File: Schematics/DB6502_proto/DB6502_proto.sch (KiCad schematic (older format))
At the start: 22 parts, among them SW1 Reset, U1 DS1813, U10 28C256, U11 22V10C, U2 74AC32, U3 65C02S, U4 74AC04, U5 62256, U6 74HC74, U7 74AC08, U8 62256, U9 74AC138, X1 14MHz

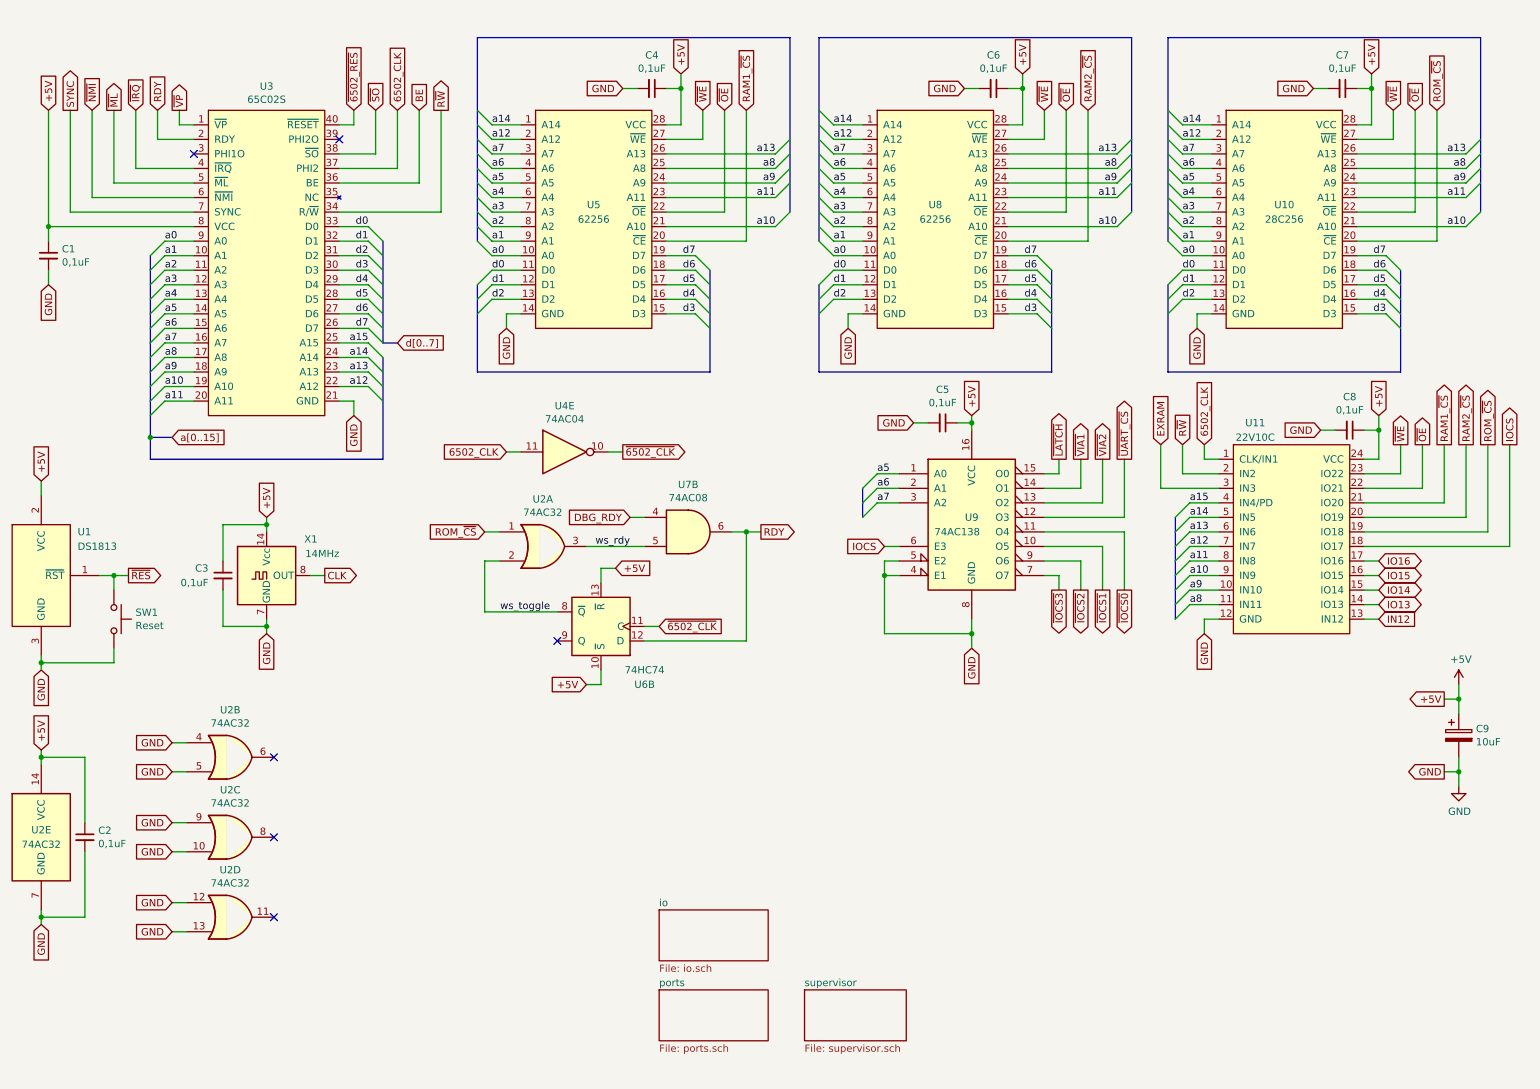
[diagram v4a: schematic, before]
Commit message: Fixed issue with UART CEN during low clock, added IRQ gate
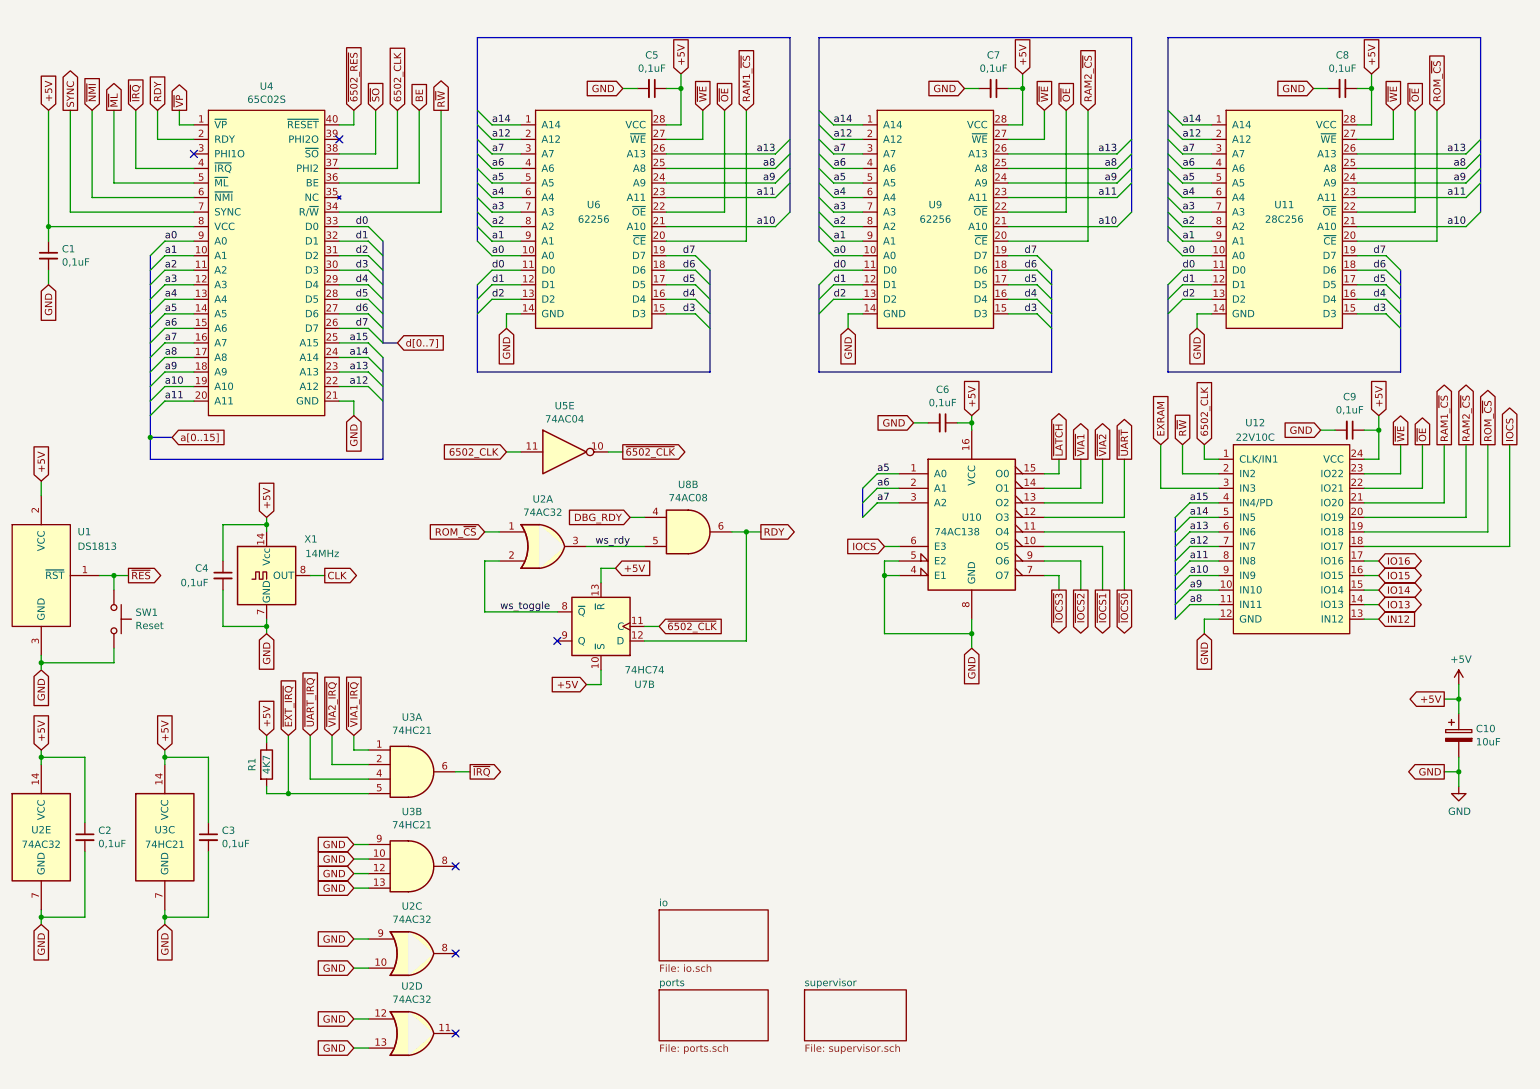
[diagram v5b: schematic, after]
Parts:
- removed unit 2 of U2
- added C3: 0,1uF, symbol Device:C_Small
- added R1: 4K7, symbol Device:R
- added U3: 74HC21, symbol 74xx:74LS21
- renumbered C9 to C10, C3 to C4, C4 to C5, C5 to C6, C6 to C7, C7 to C8, C8 to C9, U9 to U10, U10 to U11, U11 to U12, U3 to U4, U4 to U5, U5 to U6, U6 to U7, U7 to U8, U8 to U9
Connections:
- net +5V: now also C3.1, R1.1, U3.14 (VCC)
- net GND: now also C3.2, U3.10, U3.12, U3.13, U3.7 (GND), U3.9
- net ~IRQ: now also U3.6
- net ~UART_CS renamed ~UART
- new net ~EXT_IRQ: R1.2, U3.5
- new net ~UART_IRQ: U3.4
- new net ~VIA1_IRQ: U3.1
- new net ~VIA2_IRQ: U3.2
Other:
- moved on the sheet: U2C, U2D
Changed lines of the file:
@@
 	10600 5200 10600 5300
 $Comp
-L 6502:22V10C U11
+L 6502:22V10C U12
 U 1 1 5F680A6E
 P 9450 4100
-F 0 "U11" H 9200 4900 50  0000 C CNN
+F 0 "U12" H 9200 4900 50  0000 C CNN
 F 1 "22V10C" H 9200 4800 50  0000 C CNN
 F 2 "Package_DIP:DIP-24_W7.62mm_Socket" H 9450 3400 50  0001 C CNN
@@
 	8150 3850 7750 3850
 Text GLabel 8300 3550 1    50   Output ~ 0
-~UART_CS
+~UART
 Wire Wire Line
 	8300 3550 8300 3950
@@
 Connection ~ 1350 4350
 $Comp
-L 74xx:74LS138 U9
+L 74xx:74LS138 U10
 U 1 1 5F9A1F2C
 P 7250 3950
-F 0 "U9" H 7250 3950 50  0000 C CNN
+F 0 "U10" H 7250 3950 50  0000 C CNN
 F 1 "74AC138" H 7150 3850 50  0000 C CNN
 F 2 "Package_DIP:DIP-16_W7.62mm_Socket" H 7250 3950 50  0001 C CNN
@@
 $EndComp
 $Comp
-L 6502:65C02S U3
+L 6502:65C02S U4
 U 1 1 5F5A65C1
 P 2400 2150
-F 0 "U3" H 2400 3315 50  0000 C CNN
+F 0 "U4" H 2400 3315 50  0000 C CNN
 F 1 "65C02S" H 2400 3224 50  0000 C CNN
 F 2 "Package_DIP:DIP-40_W15.24mm_Socket" H 2400 3200 50  0001 C CNN
@@
 $EndComp
 $Comp
-L 6502:62256 U8
+L 6502:62256 U9
 U 1 1 5F5FD943
 P 7000 1900
-F 0 "U8" H 7000 2000 50  0000 C CNN
+F 0 "U9" H 7000 2000 50  0000 C CNN
 F 1 "62256" H 7000 1900 50  0000 C CNN
 F 2 "Package_DIP:DIP-28_W15.24mm_Socket" H 6950 2700 50  0001 C CNN
@@
 $EndComp
 $Comp
-L 6502:62256 U5
+L 6502:62256 U6
 U 1 1 5F5BE432
 P 4650 1900
-F 0 "U5" H 4650 2000 50  0000 C CNN
+F 0 "U6" H 4650 2000 50  0000 C CNN
 F 1 "62256" H 4650 1900 50  0000 C CNN
 F 2 "Package_DIP:DIP-28_W15.24mm_Socket" H 4600 2700 50  0001 C CNN
@@
 $EndComp
 $Comp
-L 6502:28C256 U10
+L 6502:28C256 U11
 U 1 1 5F605CEF
 P 9400 1900
-F 0 "U10" H 9400 2000 50  0000 C CNN
+F 0 "U11" H 9400 2000 50  0000 C CNN
 F 1 "28C256" H 9400 1900 50  0000 C CNN
 F 2 "Package_DIP:DIP-28_W15.24mm_Socket" H 9350 2700 50  0001 C CNN
@@
 P 4450 3500
 AR Path="/5F8F4E1E/5FD6D1DD" Ref="U?"  Part="5"
-AR Path="/5FD6D1DD" Ref="U4"  Part="5"
-F 0 "U4" H 4450 3817 50  0000 C CNN
+AR Path="/5FD6D1DD" Ref="U5"  Part="5"
+F 0 "U5" H 4450 3817 50  0000 C CNN
 F 1 "74AC04" H 4450 3726 50  0000 C CNN
 F 2 "" H 4450 3500 50  0001 C CNN
@@
 P 5300 4050
 AR Path="/5F8F4E1E/5FDA6F78" Ref="U?"  Part="2"
-AR Path="/5FDA6F78" Ref="U7"  Part="2"
-F 0 "U7" H 5300 4375 50  0000 C CNN
+AR Path="/5FDA6F78" Ref="U8"  Part="2"
+F 0 "U8" H 5300 4375 50  0000 C CNN
 F 1 "74AC08" H 5300 4284 50  0000 C CNN
 F 2 "" H 5300 4050 50  0001 C CNN
@@
 P 4700 4700
 AR Path="/5F8F4E1E/5FE3D22B" Ref="U?"  Part="2"
-AR Path="/5FE3D22B" Ref="U6"  Part="2"
-F 0 "U6" H 4400 5100 50  0000 C CNN
+AR Path="/5FE3D22B" Ref="U7"  Part="2"
+F 0 "U7" H 4400 5100 50  0000 C CNN
 F 1 "74HC74" H 4400 5000 50  0000 C CNN
 F 2 "" H 4700 4700 50  0001 C CNN
@@
 	900  2350 900  2250
 $Comp
-L Device:C_Small C4
+L Device:C_Small C5
 U 1 1 6006C4BF
 P 5050 1000
-F 0 "C4" V 4821 1000 50  0000 C CNN
+F 0 "C5" V 4821 1000 50  0000 C CNN
 F 1 "0,1uF" V 4912 1000 50  0000 C CNN
 F 2 "" H 5050 1000 50  0001 C CNN
@@
 	4850 1000 4950 1000
 $Comp
-L Device:C_Small C6
+L Device:C_Small C7
 U 1 1 600A0144
 P 7400 1000
-F 0 "C6" V 7171 1000 50  0000 C CNN
+F 0 "C7" V 7171 1000 50  0000 C CNN
 F 1 "0,1uF" V 7262 1000 50  0000 C CNN
 F 2 "" H 7400 1000 50  0001 C CNN
@@
 	7200 1000 7300 1000
 $Comp
-L Device:C_Small C7
+L Device:C_Small C8
 U 1 1 600B9F0E
 P 9800 1000
-F 0 "C7" V 9571 1000 50  0000 C CNN
+F 0 "C8" V 9571 1000 50  0000 C CNN
 F 1 "0,1uF" V 9662 1000 50  0000 C CNN
 F 2 "" H 9800 1000 50  0001 C CNN
@@
 +5V
 $Comp
-L Device:C_Small C8
+L Device:C_Small C9
 U 1 1 600EDE42
 P 9850 3350
-F 0 "C8" V 9621 3350 50  0000 C CNN
+F 0 "C9" V 9621 3350 50  0000 C CNN
 F 1 "0,1uF" V 9712 3350 50  0000 C CNN
 F 2 "" H 9850 3350 50  0001 C CNN
@@
 	10050 3350 10050 3250
 $Comp
-L Device:C_Small C5
+L Device:C_Small C6
 U 1 1 60156577
 P 7050 3300
-F 0 "C5" V 6821 3300 50  0000 C CNN
+F 0 "C6" V 6821 3300 50  0000 C CNN
 F 1 "0,1uF" V 6912 3300 50  0000 C CNN
 F 2 "" H 7050 3300 50  0001 C CNN
@@
 	7250 3300 7250 3350
 $Comp
-L Device:C_Small C3
+L Device:C_Small C4
 U 1 1 601720DC
 P 2100 4350
-F 0 "C3" H 2000 4400 50  0000 R CNN
+F 0 "C4" H 2000 4400 50  0000 R CNN
 F 1 "0,1uF" H 2000 4300 50  0000 R CNN
 F 2 "" H 2100 4350 50  0001 C CNN
@@
 $Comp
 L 74xx:74LS32 U2
-U 2 1 60312905
-P 2150 5600
-F 0 "U2" H 2150 5925 50  0000 C CNN
-F 1 "74AC32" H 2150 5834 50  0000 C CNN
-F 2 "" H 2150 5600 50  0001 C CNN
-F 3 "http://www.ti.com/lit/gpn/sn74LS32" H 2150 5600 50  0001 C CNN
-	2    2150 5600
-	1    0    0    -1
-$EndComp
-Text GLabel 1750 5500 0    50   Input ~ 0
-GND
-Text GLabel 1750 5700 0    50   Input ~ 0
-GND
-Wire Wire Line
-	1750 5700 1850 5700
-Wire Wire Line
-	1750 5500 1850 5500
-NoConn ~ 2450 5600
-$Comp
-L 74xx:74LS32 U2
 U 3 1 603ACD27
-P 2150 6150
-F 0 "U2" H 2150 6475 50  0000 C CNN
-F 1 "74AC32" H 2150 6384 50  0000 C CNN
-F 2 "" H 2150 6150 50  0001 C CNN
-F 3 "http://www.ti.com/lit/gpn/sn74LS32" H 2150 6150 50  0001 C CNN
-	3    2150 6150
-	1    0    0    -1
-$EndComp
-Text GLabel 1750 6050 0    50   Input ~ 0
-GND
-Text GLabel 1750 6250 0    50   Input ~ 0
-GND
-Wire Wire Line
-	1750 6250 1850 6250
-Wire Wire Line
-	1750 6050 1850 6050
-NoConn ~ 2450 6150
+P 3400 6950
+F 0 "U2" H 3400 7275 50  0000 C CNN
+F 1 "74AC32" H 3400 7184 50  0000 C CNN
+F 2 "" H 3400 6950 50  0001 C CNN
+F 3 "http://www.ti.com/lit/gpn/sn74LS32" H 3400 6950 50  0001 C CNN
+	3    3400 6950
+	1    0    0    -1
+$EndComp
+Text GLabel 3000 6850 0    50   Input ~ 0
+GND
+Text GLabel 3000 7050 0    50   Input ~ 0
+GND
+Wire Wire Line
+	3000 7050 3100 7050
+Wire Wire Line
+	3000 6850 3100 6850
+NoConn ~ 3700 6950
 $Comp
 L 74xx:74LS32 U2
 U 4 1 603CCE1F
-P 2150 6700
-F 0 "U2" H 2150 7025 50  0000 C CNN
-F 1 "74AC32" H 2150 6934 50  0000 C CNN
-F 2 "" H 2150 6700 50  0001 C CNN
-F 3 "http://www.ti.com/lit/gpn/sn74LS32" H 2150 6700 50  0001 C CNN
-	4    2150 6700
-	1    0    0    -1
-$EndComp
-Text GLabel 1750 6600 0    50   Input ~ 0
-GND
-Text GLabel 1750 6800 0    50   Input ~ 0
-GND
-Wire Wire Line
-	1750 6800 1850 6800
-Wire Wire Line
-	1750 6600 1850 6600
-NoConn ~ 2450 6700
-$Comp
-L Device:CP C9
+P 3400 7500
+F 0 "U2" H 3400 7825 50  0000 C CNN
+F 1 "74AC32" H 3400 7734 50  0000 C CNN
+F 2 "" H 3400 7500 50  0001 C CNN
+F 3 "http://www.ti.com/lit/gpn/sn74LS32" H 3400 7500 50  0001 C CNN
+	4    3400 7500
+	1    0    0    -1
+$EndComp
+Text GLabel 3000 7400 0    50   Input ~ 0
+GND
+Text GLabel 3000 7600 0    50   Input ~ 0
+GND
+Wire Wire Line
+	3000 7600 3100 7600
+Wire Wire Line
+	3000 7400 3100 7400
+NoConn ~ 3700 7500
+$Comp
+L Device:CP C10
 U 1 1 5F613640
 P 10600 5450
-F 0 "C9" H 10718 5496 50  0000 L CNN
+F 0 "C10" H 10718 5496 50  0000 L CNN
 F 1 "10uF" H 10718 5405 50  0000 L CNN
 F 2 "Capacitor_THT:CP_Radial_D4.0mm_P2.00mm" H 10638 5300 50  0001 C CNN
@@
 F1 "io.sch" 50
 $EndSheet
+$Comp
+L 74xx:74LS21 U3
+U 1 1 5FB20233
+P 3400 5700
+F 0 "U3" H 3400 6075 50  0000 C CNN
+F 1 "74HC21" H 3400 5984 50  0000 C CNN
+F 2 "" H 3400 5700 50  0001 C CNN
+F 3 "http://www.ti.com/lit/gpn/sn74LS21" H 3400 5700 50  0001 C CNN
+	1    3400 5700
+	1    0    0    -1
+$EndComp
+$Comp
+L 74xx:74LS21 U3
+U 2 1 5FB22533
+P 3400 6350
+F 0 "U3" H 3400 6725 50  0000 C CNN
+F 1 "74HC21" H 3400 6634 50  0000 C CNN
+F 2 "" H 3400 6350 50  0001 C CNN
+F 3 "http://www.ti.com/lit/gpn/sn74LS21" H 3400 6350 50  0001 C CNN
+	2    3400 6350
+	1    0    0    -1
+$EndComp
+$Comp
+L 74xx:74LS21 U3
+U 3 1 5FB2300D
+P 1700 6150
+F 0 "U3" H 1700 6200 50  0000 C CNN
+F 1 "74HC21" H 1700 6100 50  0000 C CNN
+F 2 "" H 1700 6150 50  0001 C CNN
+F 3 "http://www.ti.com/lit/gpn/sn74LS21" H 1700 6150 50  0001 C CNN
+	3    1700 6150
+	1    0    0    -1
+$EndComp
+Text GLabel 1700 5550 1    50   Input ~ 0
++5V
+Text GLabel 1700 6750 3    50   Input ~ 0
+GND
+Wire Wire Line
+	1700 6750 1700 6700
+Wire Wire Line
+	1700 5650 1700 5600
+$Comp
+L Device:C_Small C3
+U 1 1 5FB8CE95
+P 2000 6150
+F 0 "C3" H 2092 6196 50  0000 L CNN
+F 1 "0,1uF" H 2092 6105 50  0000 L CNN
+F 2 "" H 2000 6150 50  0001 C CNN
+F 3 "~" H 2000 6150 50  0001 C CNN
+	1    2000 6150
+	1    0    0    -1
+$EndComp
+Wire Wire Line
+	2000 6050 2000 5600
+Wire Wire Line
+	2000 5600 1700 5600
+Connection ~ 1700 5600
+Wire Wire Line
+	1700 5600 1700 5550
+Wire Wire Line
+	1700 6700 2000 6700
+Wire Wire Line
+	2000 6700 2000 6250
+Connection ~ 1700 6700
+Wire Wire Line
+	1700 6700 1700 6650
+Text GLabel 3000 5450 1    50   Input ~ 0
+~VIA1_IRQ
+Wire Wire Line
+	3000 5450 3000 5550
+Wire Wire Line
+	3000 5550 3100 5550
+Text GLabel 2850 5450 1    50   Input ~ 0
+~VIA2_IRQ
+Text GLabel 2700 5450 1    50   Input ~ 0
+~UART_IRQ
+Text GLabel 2550 5450 1    50   Input ~ 0
+~EXT_IRQ
+Text GLabel 3800 5700 2    50   Output ~ 0
+~IRQ
+Wire Wire Line
+	3700 5700 3800 5700
+Wire Wire Line
+	2850 5450 2850 5650
+Wire Wire Line
+	2850 5650 3100 5650
+Wire Wire Line
+	2700 5450 2700 5750
+Wire Wire Line
+	2700 5750 3100 5750
+Wire Wire Line
+	2550 5450 2550 5850
+Wire Wire Line
+	2550 5850 3100 5850
+$Comp
+L Device:R R1
+U 1 1 5FC6DB04
+P 2400 5650
+F 0 "R1" V 2300 5650 50  0000 C CNN
+F 1 "4K7" V 2400 5650 50  0000 C CNN
+F 2 "" V 2330 5650 50  0001 C CNN
+F 3 "~" H 2400 5650 50  0001 C CNN
+	1    2400 5650
+	1    0    0    -1
+$EndComp
+Text GLabel 2400 5450 1    50   Input ~ 0
++5V
+Wire Wire Line
+	2400 5450 2400 5500
+Wire Wire Line
+	2400 5800 2400 5850
+Wire Wire Line
+	2400 5850 2550 5850
+Connection ~ 2550 5850
+Text GLabel 3000 6200 0    50   Input ~ 0
+GND
+Text GLabel 3000 6300 0    50   Input ~ 0
+GND
+Text GLabel 3000 6400 0    50   Input ~ 0
+GND
+Text GLabel 3000 6500 0    50   Input ~ 0
+GND
+Wire Wire Line
+	3000 6500 3100 6500
+Wire Wire Line
+	3000 6400 3100 6400
+Wire Wire Line
+	3000 6300 3100 6300
+Wire Wire Line
+	3000 6200 3100 6200
+NoConn ~ 3700 6350
 Wire Bus Line
 	6500 3750 6500 3950

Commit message: Implemented fix for metastability issue during clock switch
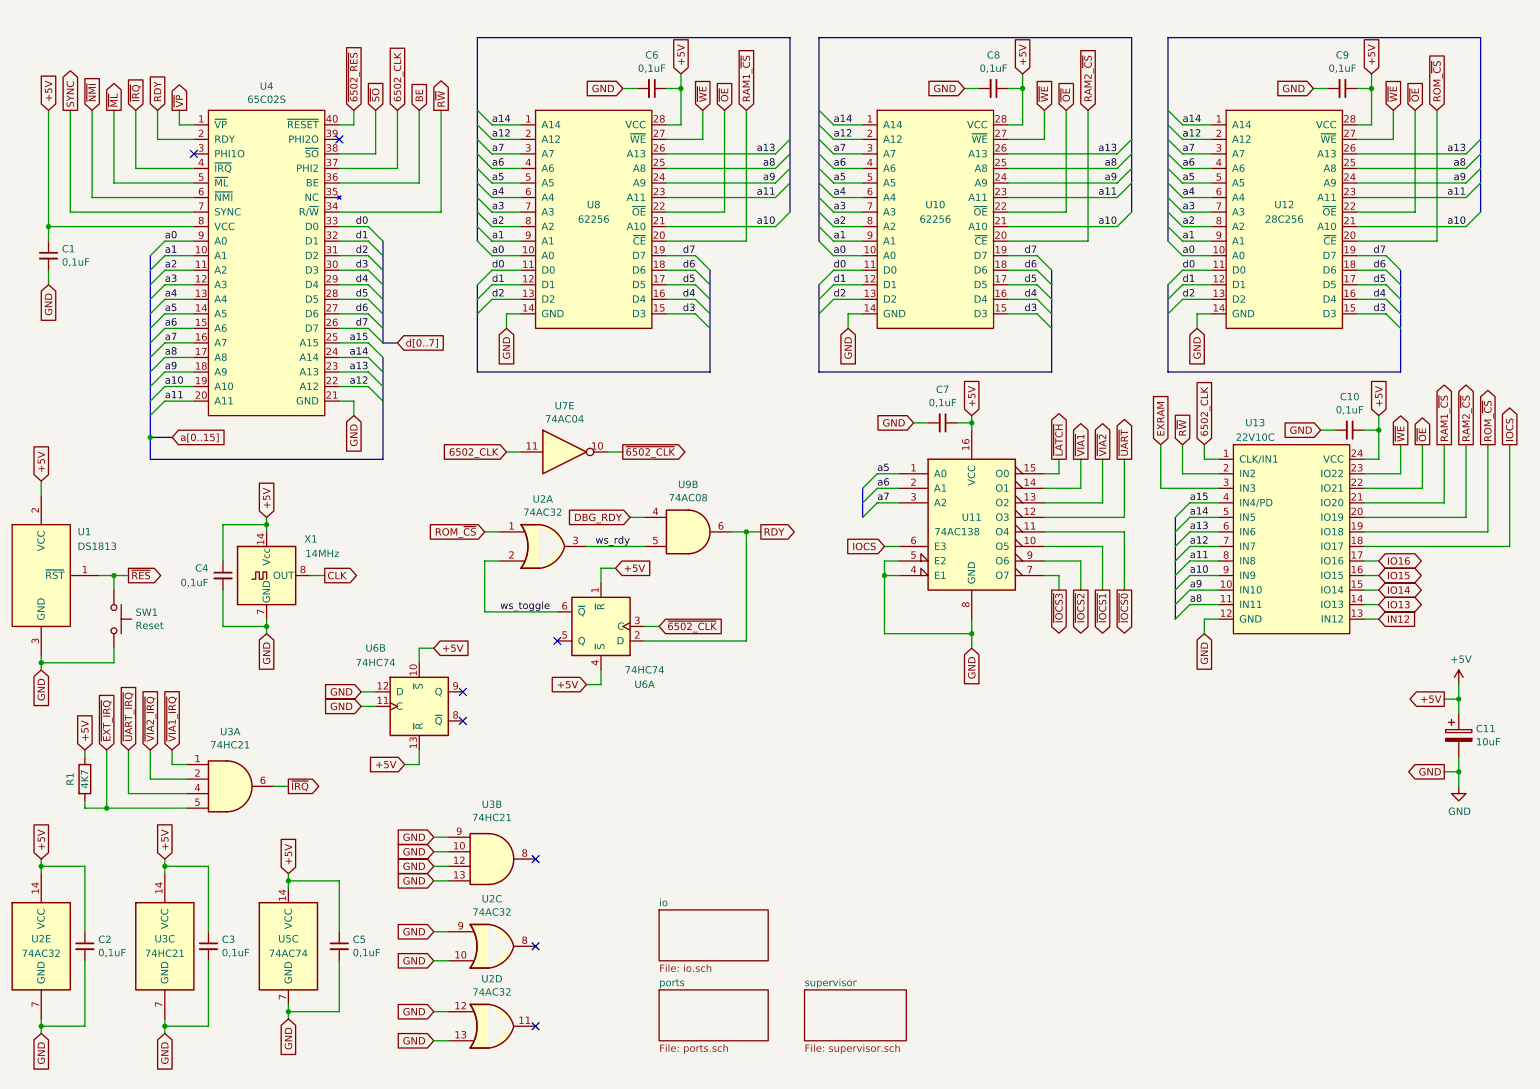
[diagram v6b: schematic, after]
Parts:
- added C5: 0,1uF, symbol Device:C_Small
- added U5: 74AC74, symbol 74xx:74HC74
- added unit 2 of U6
- renumbered C9 to C10, C10 to C11, C5 to C6, C6 to C7, C7 to C8, C8 to C9, U9 to U10, U10 to U11, U11 to U12, U12 to U13, U7 to U6, U5 to U7, U6 to U8, U8 to U9
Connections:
- net +5V: now also U6.1 (~R), U6.4 (~S), C5.1, U5.14 (VCC), U6.10 (~S), U6.13 (~R); no longer U6.10 (~S), U6.13 (~R)
- net GND: now also C5.2, U5.7 (GND), U6.11 (C), U6.12 (D)
- net RDY: now also U6.2 (D); no longer U6.12 (D)
- net ws_toggle: now also U6.6 (~Q); no longer U6.8 (~Q)
- net ~6502_CLK: now also U6.3 (C); no longer U6.11 (C)
- no-connect marks 6 -> 8
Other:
- moved on the sheet: C2, C3, R1, U2C, U2D, U2E, U3A, U3B, U3C
